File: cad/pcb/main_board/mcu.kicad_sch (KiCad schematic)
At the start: 13 parts, among them J2 Conn_ARM_JTAG_SWD_10, U1 STM32F401R_B-C_Tx, Y1 Crystal_GND23

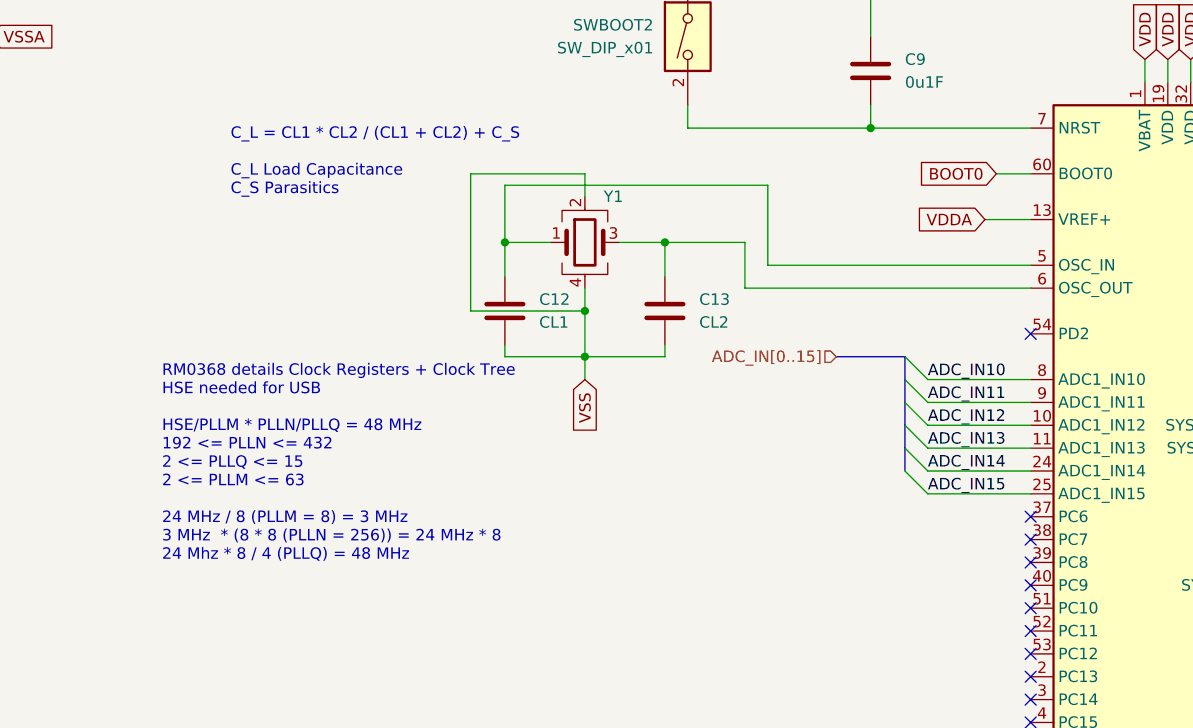
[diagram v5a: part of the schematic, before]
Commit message: SWD connector start
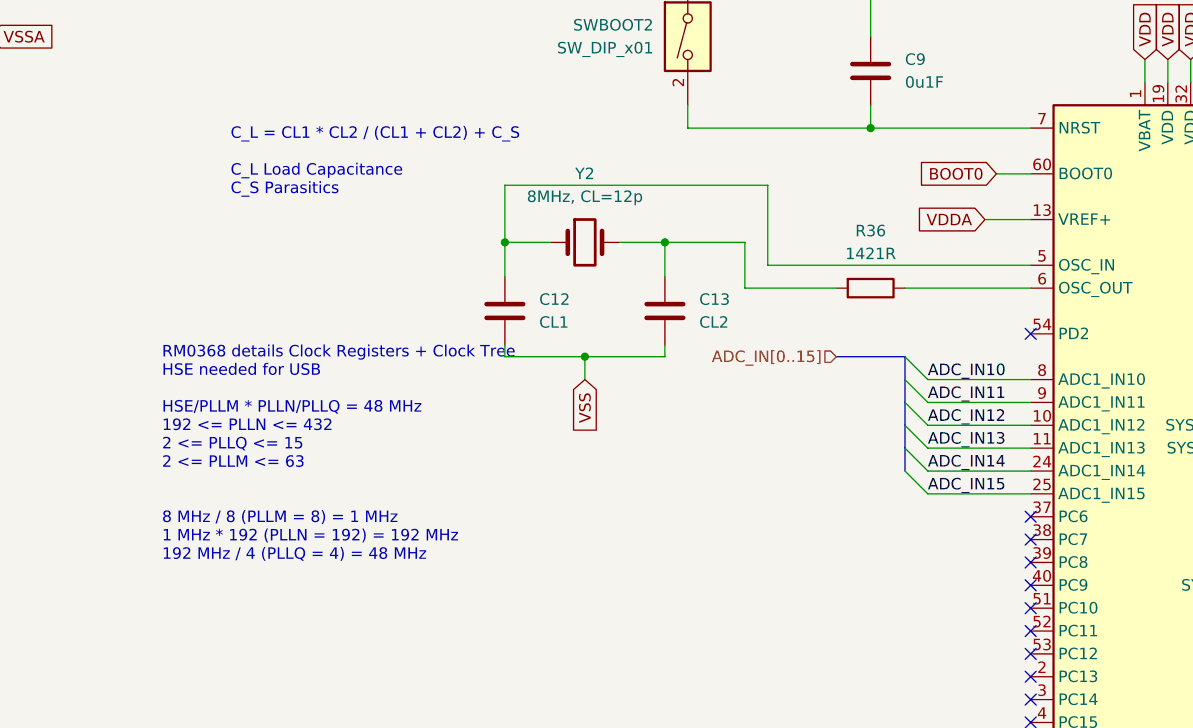
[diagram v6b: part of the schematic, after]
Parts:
- removed Y1: Crystal_GND23, Crystal:Crystal_SMD_2016-4Pin_2.0x1.6mm, symbol Device:Crystal_GND24
- added R36: 1421R, Resistor_SMD:R_0805_2012Metric, symbol Device:R
- added Y2: 8MHz, CL=12p, local:FC4SDCBMF8.0-T1, symbol Device:Crystal
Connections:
- net at C12.1, U1.5 (PH0): now also Y2.1
- net at U1.6 (PH1): now also R36.1; no longer C13.1
- new net: C13.1, R36.2, Y2.2
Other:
- note added: "RM0368 details Clock Registers + Clock Tree HSE needed for USB HSE/PLLM * PLLN/PLLQ = 48 MHz 192 <= PLLN <= 432 2 <= PLLQ <= 15 2 <= PLLM <= 63 8 MHz / 8 (PLLM = 8) = 1 MHz 1 MHz * 192 (PLLN = 192) = 192 MHz 192 MHz / 4 (PLLQ = 4) = 48 MHz"
- note removed: "RM0368 details Clock Registers + Clock Tree HSE needed for USB HSE/PLLM * PLLN/PLLQ = 48 MHz 192 <= PLLN <= 432 2 <= PLLQ <= 15 2 <= PLLM <= 63 24 MHz / 8 (PLLM = 8) = 3 MHz 3 MHz * (8 * 8 (PLLN = 256)) = 24 MHz * 8 24 Mhz * 8 / 4 (PLLQ) = 48 MHz"
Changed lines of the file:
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@@
-	)
-	(junction
-		(at 102.87 80.01)
-		(diameter 0)
-		(color 0 0 0 0)
 	)
 	(junction
@@
 	(wire
 		(pts
+			(xy 130.81 77.47) (xy 120.65 77.47)
+		)
+		(stroke
+			(width 0)
+			(type default)
+		)
+	)
+	(wire
+		(pts
 			(xy 185.42 85.09) (xy 187.96 85.09)
 		)
@@
 	(wire
 		(pts
-			(xy 102.87 80.01) (xy 102.87 85.09)
-		)
-		(stroke
-			(width 0)
-			(type default)
-		)
-	)
-	(wire
-		(pts
 			(xy 185.42 74.93) (xy 195.58 74.93)
 		)
@@
 	(wire
 		(pts
-			(xy 102.87 80.01) (xy 102.87 77.47)
-		)
-		(stroke
-			(width 0)
-			(type default)
-		)
-	)
-	(wire
-		(pts
 			(xy 232.41 110.49) (xy 224.79 110.49)
 		)
@@
 	(wire
 		(pts
-			(xy 90.17 80.01) (xy 102.87 80.01)
-		)
-		(stroke
-			(width 0)
-			(type default)
-		)
-	)
-	(wire
-		(pts
 			(xy 134.62 59.69) (xy 134.62 57.15)
 		)
@@
 	(wire
 		(pts
-			(xy 102.87 64.77) (xy 90.17 64.77)
-		)
-		(stroke
-			(width 0)
-			(type default)
-		)
-	)
-	(wire
-		(pts
 			(xy 170.18 146.05) (xy 170.18 149.86)
 		)
@@
 	(wire
 		(pts
-			(xy 152.4 77.47) (xy 120.65 77.47)
-		)
-		(stroke
-			(width 0)
-			(type default)
-		)
-	)
-	(wire
-		(pts
-			(xy 102.87 67.31) (xy 102.87 64.77)
+			(xy 152.4 77.47) (xy 138.43 77.47)
 		)
 		(stroke
@@
 		(pts
 			(xy 102.87 85.09) (xy 102.87 87.63)
-		)
-		(stroke
-			(width 0)
-			(type default)
-		)
-	)
-	(wire
-		(pts
-			(xy 90.17 64.77) (xy 90.17 80.01)
 		)
 		(stroke
@@
 		)
 	)
-	(text "RM0368 details Clock Registers + Clock Tree\nHSE needed for USB\n\nHSE/PLLM * PLLN/PLLQ = 48 MHz\n192 <= PLLN <= 432\n2 <= PLLQ <= 15\n2 <= PLLM <= 63\n\n24 MHz / 8 (PLLM = 8) = 3 MHz\n3 MHz  * (8 * 8 (PLLN = 256)) = 24 MHz * 8\n24 Mhz * 8 / 4 (PLLQ) = 48 MHz"
+	(text "RM0368 details Clock Registers + Clock Tree\nHSE needed for USB\n\nHSE/PLLM * PLLN/PLLQ = 48 MHz\n192 <= PLLN <= 432\n2 <= PLLQ <= 15\n2 <= PLLM <= 63\n\n\n8 MHz / 8 (PLLM = 8) = 1 MHz\n1 MHz * 192 (PLLN = 192) = 192 MHz\n192 MHz / 4 (PLLQ = 4) = 48 MHz"
 		(exclude_from_sim no)
 		(at 55.88 107.95 0)
@@
 	)
 	(symbol
-		(lib_id "Device:Crystal_GND24")
-		(at 102.87 72.39 0)
-		(unit 1)
-		(exclude_from_sim no)
-		(in_bom yes)
-		(on_board yes)
-		(dnp no)
-		(property "Reference" "Y1"
-			(at 106.045 67.31 0)
-			(effects
-				(font
-					(size 1.27 1.27)
-				)
-			)
-		)
-		(property "Value" "Crystal_GND23"
-			(at 111.125 77.47 0)
-			(effects
-				(font
-					(size 1.27 1.27)
-				)
-				(hide yes)
-			)
-		)
-		(property "Footprint" "Crystal:Crystal_SMD_2016-4Pin_2.0x1.6mm"
-			(at 102.87 72.39 0)
-			(effects
-				(font
-					(size 1.27 1.27)
-				)
-				(hide yes)
-			)
-		)
-		(property "Datasheet" "~"
-			(at 102.87 72.39 0)
-			(effects
-				(font
-					(size 1.27 1.27)
-				)
-				(hide yes)
-			)
-		)
-		(property "Description" "Four pin crystal, GND on pins 2 and 4"
-			(at 102.87 72.39 0)
-			(effects
-				(font
-					(size 1.27 1.27)
-				)
-				(hide yes)
-			)
-		)
-		(pin "1"
-		)
-		(pin "2"
-		)
-		(pin "3"
-		)
-		(pin "4"
-		)
-		(instances
-			(project "main_board"
-				(path "/6c1b8035-64fa-4797-a506-5c9583cb241c/89e1b759-e3da-4961-90e8-6f92bf79e795"
-					(reference "Y1")
-					(unit 1)
-				)
-			)
-		)
-	)
-	(symbol
 		(lib_id "Device:C")
 		(at 260.35 130.81 0)
@@
 	)
 	(symbol
+		(lib_id "Device:Crystal")
+		(at 102.87 72.39 0)
+		(unit 1)
+		(exclude_from_sim no)
+		(in_bom yes)
+		(on_board yes)
+		(dnp no)
+		(fields_autoplaced yes)
+		(property "Reference" "Y2"
+			(at 102.87 64.77 0)
+			(effects
+				(font
+					(size 1.27 1.27)
+				)
+			)
+		)
+		(property "Value" "8MHz, CL=12p"
+			(at 102.87 67.31 0)
+			(effects
+				(font
+					(size 1.27 1.27)
+				)
+			)
+		)
+		(property "Footprint" "local:FC4SDCBMF8.0-T1"
+			(at 102.87 72.39 0)
+			(effects
+				(font
+					(size 1.27 1.27)
+				)
+				(hide yes)
+			)
+		)
+		(property "Datasheet" "~"
+			(at 102.87 72.39 0)
+			(effects
+				(font
+					(size 1.27 1.27)
+				)
+				(hide yes)
+			)
+		)
+		(property "Description" "Two pin crystal"
+			(at 102.87 72.39 0)
+			(effects
+				(font
+					(size 1.27 1.27)
+				)
+				(hide yes)
+			)
+		)
+		(pin "1"
+		)
+		(pin "2"
+		)
+		(instances
+			(project ""
+				(path "/6c1b8035-64fa-4797-a506-5c9583cb241c/89e1b759-e3da-4961-90e8-6f92bf79e795"
+					(reference "Y2")
+					(unit 1)
+				)
+			)
+		)
+	)
+	(symbol
 		(lib_id "Device:C")
 		(at 111.76 80.01 0)
@@
 					(unit 1)
 				)
+			)
+		)
+	)
+	(symbol
+		(lib_id "Device:R")
+		(at 134.62 77.47 270)
+		(unit 1)
+		(exclude_from_sim no)
+		(in_bom yes)
+		(on_board yes)
+		(dnp no)
+		(fields_autoplaced yes)
+		(property "Reference" "R36"
+			(at 134.62 71.12 90)
+			(effects
+				(font
+					(size 1.27 1.27)
+				)
+			)
+		)
+		(property "Value" "1421R"
+			(at 134.62 73.66 90)
+			(effects
+				(font
+					(size 1.27 1.27)
+				)
+			)
+		)
+		(property "Footprint" "Resistor_SMD:R_0805_2012Metric"
+			(at 134.62 75.692 90)
+			(effects
+				(font
+					(size 1.27 1.27)
+				)
+				(hide yes)
+			)
+		)
+		(property "Datasheet" "~"
+			(at 134.62 77.47 0)
+			(effects
+				(font
+					(size 1.27 1.27)
+				)
+				(hide yes)
+			)
+		)
+		(property "Description" "Resistor"
+			(at 134.62 77.47 0)
+			(effects
+				(font
+					(size 1.27 1.27)
+				)
+				(hide yes)
+			)
+		)
+		(pin "1"
+		)
+		(pin "2"
+		)
+		(instances
+			(project ""
+				(path "/6c1b8035-64fa-4797-a506-5c9583cb241c/89e1b759-e3da-4961-90e8-6f92bf79e795"
+					(reference "R36")
+					(unit 1)
+				)
